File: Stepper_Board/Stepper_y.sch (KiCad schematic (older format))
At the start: 14 parts

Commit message: Testsoftware for ImageProcessing in c programmiert
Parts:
- removed C?: 2.2u 16V, Capacitor_SMD:C_0603_1608Metric, symbol Device:C_Small
- removed C?: 22n 50V, Capacitor_SMD:C_0603_1608Metric, symbol Device:C_Small
- removed C? (x3): 100n 50V, Capacitor_SMD:C_0603_1608Metric, symbol Device:C_Small
- removed C? (x2): 100u 35V, Capacitor_THT:CP_Radial_D6.3mm_P2.50mm, symbol Device:CP_Small
- removed C?: 1u 16V, Capacitor_SMD:C_0603_1608Metric, symbol Device:C_Small
- removed R?: 0.22R 0.5W, Resistor_SMD:R_1210_3225Metric, symbol Device:R_Small
- removed R?: 22k, Resistor_SMD:R_0603_1608Metric, symbol Device:R_Small
- removed SW?: SW_DIP_x03, Package_DIP:DIP-6_W7.62mm, symbol Switch:SW_DIP_x03
- removed U?: TMC2226, Package_SO:TSSOP-28-1EP_4.4x9.7mm_P0.65mm, symbol Pick_n_Place:TMC2226
- added C302: 2.2u 16V, Capacitor_SMD:C_0603_1608Metric, symbol Device:C_Small
- added C303: 1u 16V, Capacitor_SMD:C_0603_1608Metric, symbol Device:C_Small
- added C304: 22n 50V, Capacitor_SMD:C_0603_1608Metric, symbol Device:C_Small
- added C305, C306, C307: 100n 50V, Capacitor_SMD:C_0603_1608Metric, symbol Device:C_Small
- added C308, C309: 100u 35V, Capacitor_THT:CP_Radial_D6.3mm_P2.50mm, symbol Device:CP_Small
- added R301: 22k, Resistor_SMD:R_0603_1608Metric, symbol Device:R_Small
- added R302: 0.1R 0.5W, Resistor_SMD:R_1210_3225Metric, symbol Device:R_Small
- added SW301: SW_DIP_x03, Package_DIP:DIP-6_W7.62mm, symbol Switch:SW_DIP_x03
- added U301: TMC2226-Pick_n_Place, Package_SO:TSSOP-28-1EP_4.4x9.7mm_P0.65mm, symbol StepperBoard-rescue:TMC2226-Pick_n_Place
- R303: renamed from R?; value 0.22R 0.5W -> 0.1R 0.5W; LCSC C159293 -> C270892
- gave numbers to parts that had none: 1
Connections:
- net labels added: CUR_CONTROL_X, DIAG_X, DIR_X, EN_X, INDEX_X, OA1_X, OA2_X, OB1_X, OB2_X, STEP_X
- net labels removed: CUR_CONTROL, DIAG, DIR, EN, INDEX, OA1, OA2, OB1, OB2, STEP
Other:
- note added: "1920mA"
- note removed: "100mOhm C270892"
- note removed: "960mA"

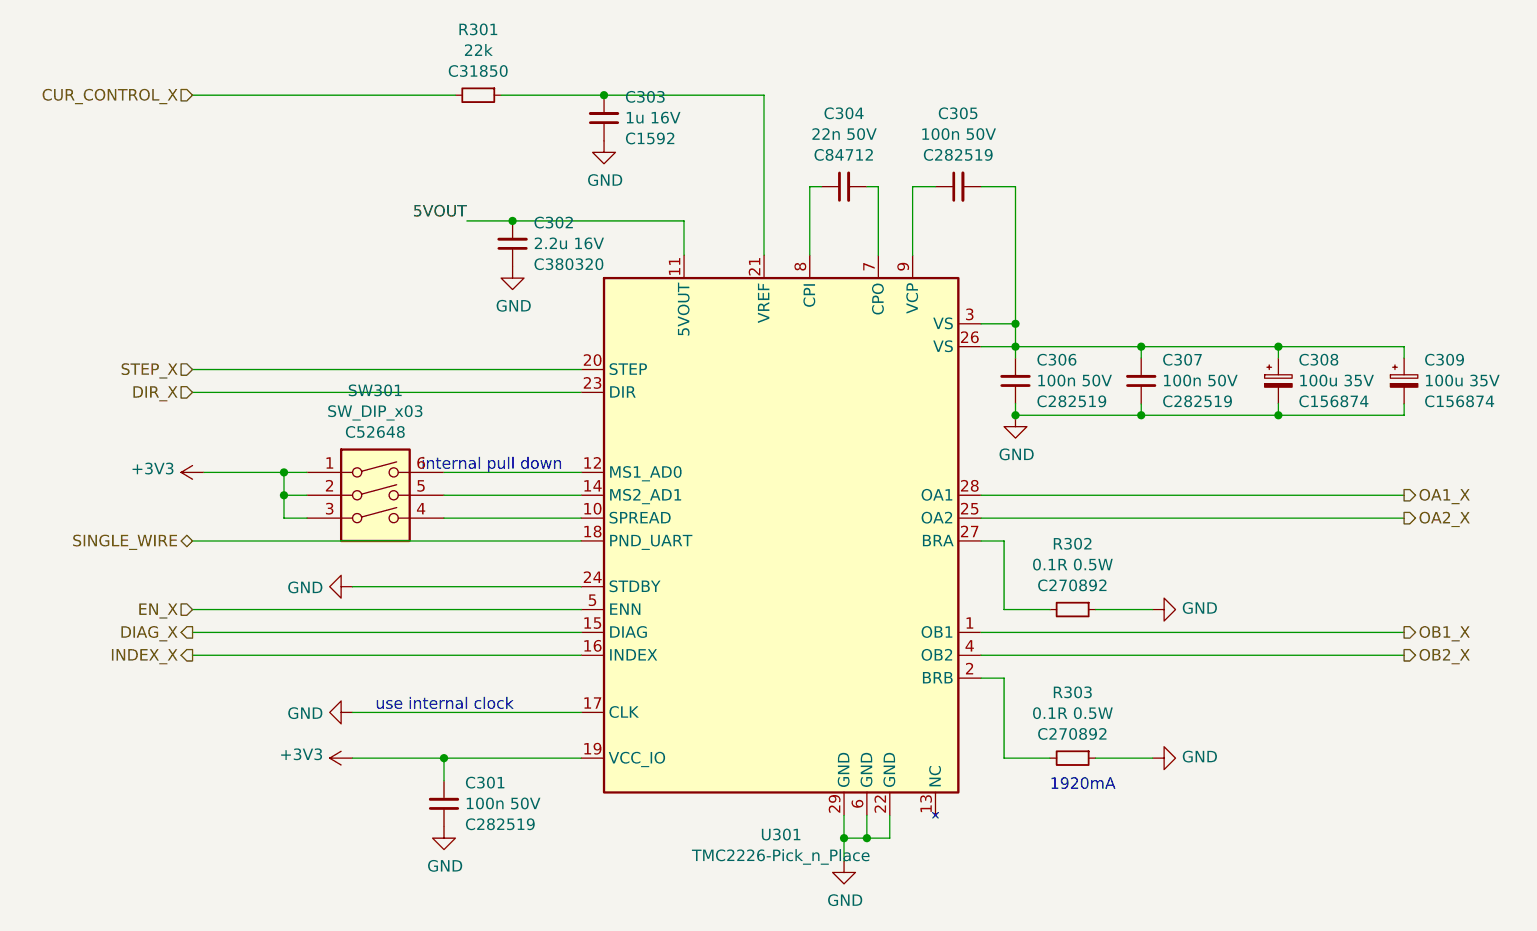
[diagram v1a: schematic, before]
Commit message: STM32F401 für motoransteuerung gewählt. TODO: motoransteuerung und leistungsteil trennen, damit für schnelle fehlerbehebung modul getauscht werden kann
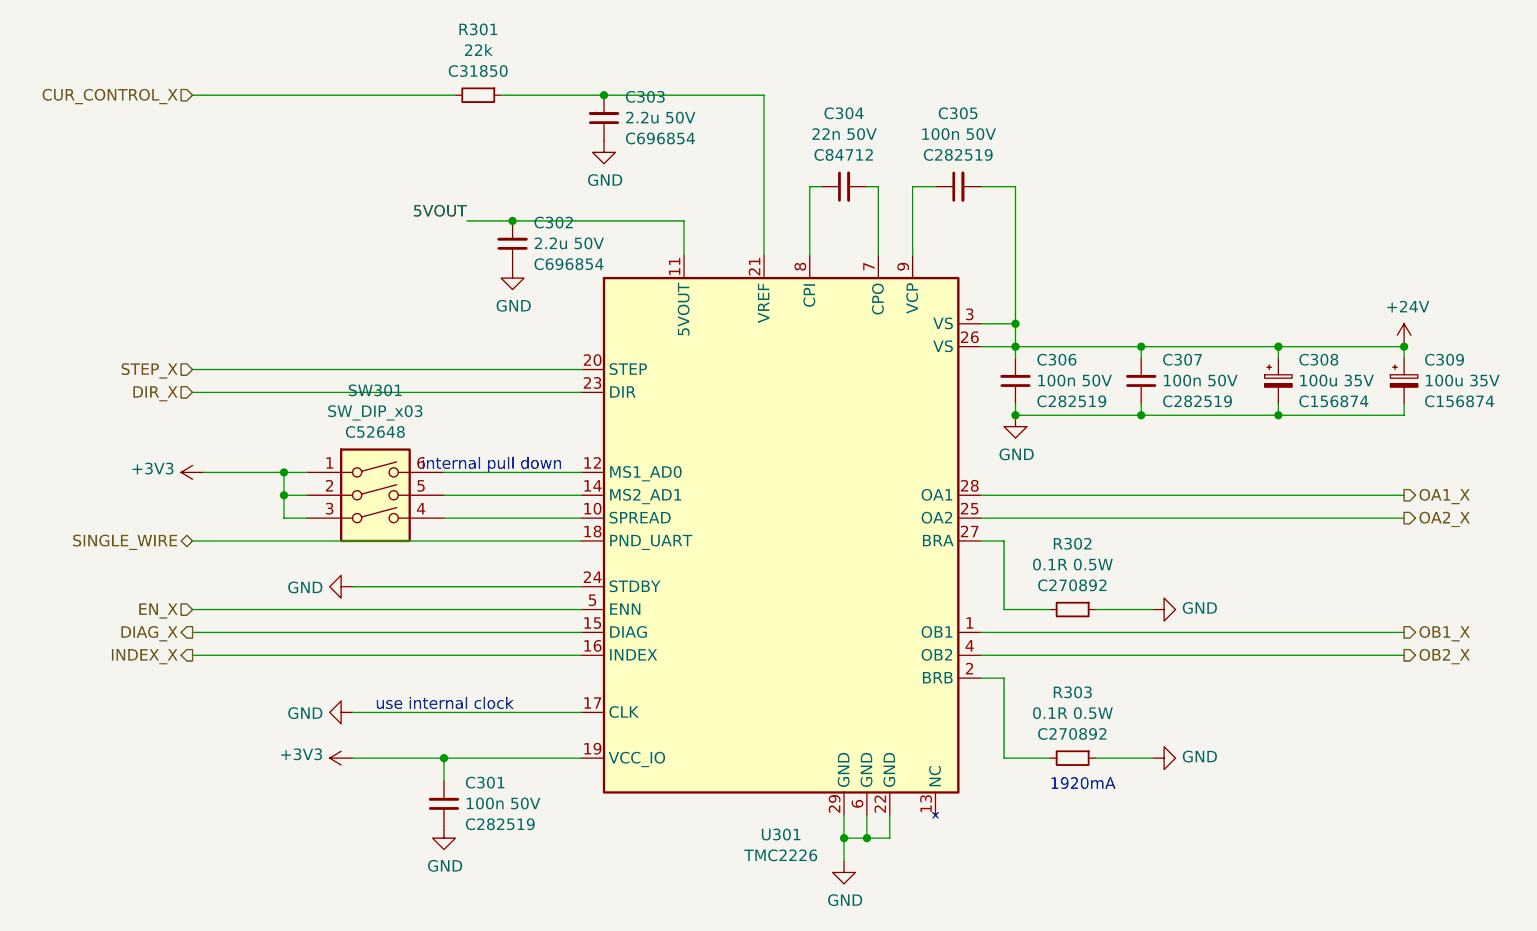
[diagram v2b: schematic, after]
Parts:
- C302: value 2.2u 16V -> 2.2u 50V; footprint Capacitor_SMD:C_0603_1608Metric -> Capacitor_SMD:C_1210_3225Metric; LCSC C380320 -> C696854
- C303: value 1u 16V -> 2.2u 50V; footprint Capacitor_SMD:C_0603_1608Metric -> Capacitor_SMD:C_1210_3225Metric; LCSC C1592 -> C696854
- U301: value TMC2226-Pick_n_Place -> TMC2226; LCSC (none) -> C705366
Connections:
- net +24V: now reaches C305.2, C306.2, C307.2, C308.1, C309.1, U301.26 (VS), U301.3 (VS)
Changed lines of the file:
@@
 AR Path="/5FCAEEEC/5FCB6219" Ref="C?"  Part="1"
 F 0 "C302" H 5458 1509 50  0000 R CNN
-F 1 "2.2u 16V" H 5458 1600 50  0000 R CNN
-F 2 "Capacitor_SMD:C_0603_1608Metric" H 5550 1600 50  0001 C CNN
+F 1 "2.2u 50V" H 5458 1600 50  0000 R CNN
+F 2 "Capacitor_SMD:C_1210_3225Metric" H 5550 1600 50  0001 C CNN
 F 3 "~" H 5550 1600 50  0001 C CNN
-F 4 "C380320 " H 5458 1691 50  0000 R CNN "LCSC"
+F 4 " C696854 " H 5458 1691 50  0000 R CNN "LCSC"
 	1    5550 1600
 	-1   0    0    1
@@
 AR Path="/5FCAEEEC/5FCB6246" Ref="C?"  Part="1"
 F 0 "C303" H 5858 959 50  0000 R CNN
-F 1 "1u 16V" H 5858 1050 50  0000 R CNN
-F 2 "Capacitor_SMD:C_0603_1608Metric" H 5950 1050 50  0001 C CNN
+F 1 "2.2u 50V" H 5858 1050 50  0000 R CNN
+F 2 "Capacitor_SMD:C_1210_3225Metric" H 5950 1050 50  0001 C CNN
 F 3 "~" H 5950 1050 50  0001 C CNN
-F 4 "C1592" H 5858 1141 50  0000 R CNN "LCSC"
+F 4 " C696854 " H 5858 1141 50  0000 R CNN "LCSC"
 	1    5950 1050
 	-1   0    0    1
@@
 AR Path="/5FCAEEEC/5FCAEB1B" Ref="U?"  Part="1"
 F 0 "U301" H 6725 1114 50  0000 C CNN
-F 1 "TMC2226-Pick_n_Place" H 6725 1023 50  0000 C CNN
+F 1 "TMC2226" H 6725 1023 50  0000 C CNN
 F 2 "Package_SO:TSSOP-28-1EP_4.4x9.7mm_P0.65mm" H 6700 850 50  0001 C CNN
 F 3 "" H 5300 3700 50  0001 C CNN
+F 4 "C705366" H 0   0   50  0001 C CNN "LCSC"
 	1    6450 2650
 	1    0    0    -1
 $EndComp
+$Comp
+L power:+24V #PWR0301
+U 1 1 600507C0
+P 9450 2050
+F 0 "#PWR0301" H 9450 1900 50  0001 C CNN
+F 1 "+24V" H 9465 2223 50  0000 C CNN
+F 2 "" H 9450 2050 50  0001 C CNN
+F 3 "" H 9450 2050 50  0001 C CNN
+	1    9450 2050
+	1    0    0    -1
+$EndComp
+Connection ~ 9450 2050
 $EndSCHEMATC
